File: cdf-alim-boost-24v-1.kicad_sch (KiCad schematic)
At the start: 89 parts, among them J1 Conn_01x02, J2 Conn_01x02, J3 Conn_01x02, Q1 BSC019N04LS, Q2 BSC019N04LS, Q3 BSC019N04LS, Q4 BSC019N04LS, Q5 BSC019N04LS, U1 HT753-1, U2 TPS25983, U4 LM5122

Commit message: schem: add boost shunt filter rc
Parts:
- added C34: 0n1, Capacitor_SMD:C_0402_1005Metric, symbol Device:C
- added R24, R25: 100, Resistor_SMD:R_0402_1005Metric, symbol Device:R
- C24: footprint Capacitor_SMD:C_0603_1608Metric_Pad1.08x0.95mm_HandSolder -> Resistor_SMD:R_0603_1608Metric
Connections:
- net +18V: now also R24.1; no longer U4.4 (CSP)
- net at L1.1, R16.2, TP12.1: now also R25.1; no longer U4.3 (CSN)
- new net: C34.2, R25.2, U4.3 (CSN)
- new net: C34.1, R24.2, U4.4 (CSP)

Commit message: schem: remove ilim testpoint
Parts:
- removed TP8: TestPoint, TestPoint:TestPoint_Pad_D2.0mm, symbol Connector:TestPoint_Small
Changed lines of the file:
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@@
 	)
 	(junction
-		(at 78.74 104.14)
-		(diameter 0)
-		(color 0 0 0 0)
-	)
-	(junction
 		(at 123.19 29.21)
 		(diameter 0)
@@
 					(unit 1)
 				)
-			)
-		)
-	)
-	(symbol
-		(lib_id "Connector:TestPoint_Small")
-		(at 78.74 104.14 270)
-		(unit 1)
-		(body_style 1)
-		(exclude_from_sim no)
-		(in_bom no)
-		(on_board yes)
-		(in_pos_files yes)
-		(dnp no)
-		(property "Reference" "TP8"
-			(at 73.66 102.87 90)
-			(show_name no)
-			(do_not_autoplace no)
-			(effects
-				(font
-					(size 1.27 1.27)
-				)
-				(justify left)
-			)
-		)
-		(property "Value" "TestPoint"
-			(at 80.7721 106.68 0)
-			(hide yes)
-			(show_name no)
-			(do_not_autoplace no)
-			(effects
-				(font
-					(size 1.27 1.27)
-				)
-				(justify left)
-			)
-		)
-		(property "Footprint" "TestPoint:TestPoint_Pad_D2.0mm"
-			(at 78.74 109.22 0)
-			(hide yes)
-			(show_name no)
-			(do_not_autoplace no)
-			(effects
-				(font
-					(size 1.27 1.27)
-				)
-			)
-		)
-		(property "Datasheet" ""
-			(at 78.74 109.22 0)
-			(hide yes)
-			(show_name no)
-			(do_not_autoplace no)
-			(effects
-				(font
-					(size 1.27 1.27)
-				)
-			)
-		)
-		(property "Description" "test point"
-			(at 78.74 104.14 0)
-			(hide yes)
-			(show_name no)
-			(do_not_autoplace no)
-			(effects
-				(font
-					(size 1.27 1.27)
-				)
-			)
-		)
-		(pin "1"
-		)
-		(instances
-			(project "cdf-alim-boost-24v-1"
-				(path "/c1d68e1e-31aa-4338-bfd5-3714fe43b2c6"
-					(reference "TP8")
-					(unit 1)
-				)

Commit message: schem: add assembly and mounting holes
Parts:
- added FID1, FID2, FID3: Fiducial, Fiducial:Fiducial_1mm_Mask2mm, symbol Mechanical:Fiducial
- added H1, H2, H3: MountingHole, MountingHole:ToolingHole_1.152mm, symbol Mechanical:MountingHole
- added H4, H5, H6, H7: MountingHole_Pad, MountingHole:MountingHole_3.2mm_M3_Pad_Via, symbol Mechanical:MountingHole_Pad
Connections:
- net AGND: now also H4.1, H5.1, H6.1, H7.1
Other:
- note added: "Mounting"
- note added: "SMT assembly"

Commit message: schem: remove extra +18v testpoint
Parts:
- removed TP11: TestPoint, TestPoint:TestPoint_Pad_D2.0mm, symbol Connector:TestPoint
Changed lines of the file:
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@@
 	)
 	(junction
-		(at 143.51 29.21)
-		(diameter 0)
-		(color 0 0 0 0)
-	)
-	(junction
 		(at 95.25 29.21)
 		(diameter 0)
@@
 	(wire
 		(pts
-			(xy 123.19 29.21) (xy 143.51 29.21)
-		)
-		(stroke
-			(width 0)
-			(type default)
-		)
-	)
-	(wire
-		(pts
 			(xy 31.75 38.1) (xy 31.75 39.37)
 		)
@@
 	(wire
 		(pts
-			(xy 143.51 29.21) (xy 156.21 29.21)
+			(xy 123.19 29.21) (xy 156.21 29.21)
 		)
 		(stroke
@@
 					(unit 1)
 				)
-			)
-		)
-	)
-	(symbol
-		(lib_id "Connector:TestPoint")
-		(at 143.51 29.21 0)
-		(unit 1)
-		(body_style 1)
-		(exclude_from_sim no)
-		(in_bom no)
-		(on_board yes)
-		(in_pos_files yes)
-		(dnp no)
-		(property "Reference" "TP11"
-			(at 141.986 23.876 0)
-			(show_name no)
-			(do_not_autoplace no)
-			(effects
-				(font
-					(size 1.27 1.27)
-				)
-				(justify left)
-			)
-		)
-		(property "Value" "TestPoint"
-			(at 146.05 27.1779 0)
-			(hide yes)
-			(show_name no)
-			(do_not_autoplace no)
-			(effects
-				(font
-					(size 1.27 1.27)
-				)
-				(justify left)
-			)
-		)
-		(property "Footprint" "TestPoint:TestPoint_Pad_D2.0mm"
-			(at 148.59 29.21 0)
-			(hide yes)
-			(show_name no)
-			(do_not_autoplace no)
-			(effects
-				(font
-					(size 1.27 1.27)
-				)
-			)
-		)
-		(property "Datasheet" ""
-			(at 148.59 29.21 0)
-			(hide yes)
-			(show_name no)
-			(do_not_autoplace no)
-			(effects
-				(font
-					(size 1.27 1.27)
-				)
-			)
-		)
-		(property "Description" "test point"
-			(at 143.51 29.21 0)
-			(hide yes)
-			(show_name no)
-			(do_not_autoplace no)
-			(effects
-				(font
-					(size 1.27 1.27)
-				)
-			)
-		)
-		(pin "1"
-		)
-		(instances
-			(project "cdf-alim-boost-24v-1"
-				(path "/c1d68e1e-31aa-4338-bfd5-3714fe43b2c6"
-					(reference "TP11")
-					(unit 1)
-				)

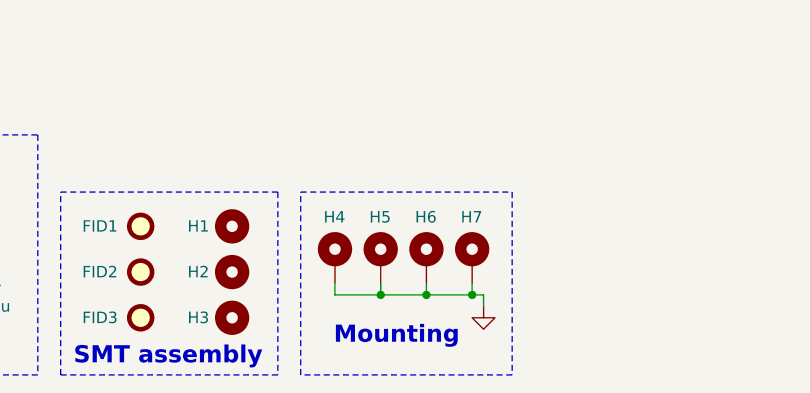
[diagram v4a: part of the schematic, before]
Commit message: schem: remove 1 mouting hole
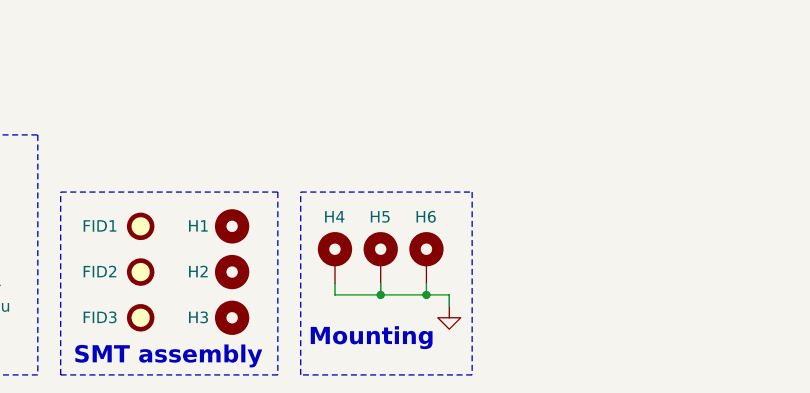
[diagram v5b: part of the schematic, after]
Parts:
- removed H7: MountingHole_Pad, MountingHole:MountingHole_3.2mm_M3_Pad_Via, symbol Mechanical:MountingHole_Pad
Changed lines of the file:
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@@
 	(rectangle
 		(start 87.63 175.26)
-		(end 111.125 195.58)
+		(end 106.68 195.58)
 		(stroke
 			(width 0)
@@
 	(text "Mounting"
 		(exclude_from_sim no)
-		(at 98.298 191.262 0)
+		(at 95.504 191.516 0)
 		(effects
 			(font
@@
 	)
 	(junction
-		(at 106.68 186.69)
-		(diameter 0)
-		(color 0 0 0 0)
-	)
-	(junction
 		(at 48.26 104.14)
 		(diameter 0)
@@
 	(wire
 		(pts
-			(xy 106.68 185.42) (xy 106.68 186.69)
-		)
-		(stroke
-			(width 0)
-			(type default)
-		)
-	)
-	(wire
-		(pts
 			(xy 213.36 29.21) (xy 218.44 29.21)
 		)
@@
 	(wire
 		(pts
-			(xy 106.68 186.69) (xy 107.95 186.69)
-		)
-		(stroke
-			(width 0)
-			(type default)
-		)
-	)
-	(wire
-		(pts
 			(xy 91.44 186.69) (xy 96.52 186.69)
 		)
@@
 	(wire
 		(pts
-			(xy 107.95 186.69) (xy 107.95 187.96)
+			(xy 104.14 186.69) (xy 104.14 187.96)
 		)
 		(stroke
@@
 	(wire
 		(pts
-			(xy 96.52 186.69) (xy 106.68 186.69)
+			(xy 96.52 186.69) (xy 104.14 186.69)
 		)
 		(stroke
@@
 	(symbol
 		(lib_id "power:GND")
-		(at 107.95 187.96 0)
+		(at 104.14 187.96 0)
 		(unit 1)
 		(body_style 1)
@@
 		(dnp no)
 		(property "Reference" "#PWR051"
-			(at 107.95 194.31 0)
+			(at 104.14 194.31 0)
 			(hide yes)
 			(show_name no)
@@
 		)
 		(property "Value" "GND"
-			(at 107.696 192.532 0)
+			(at 103.886 192.532 0)
 			(hide yes)
 			(show_name no)
@@
 		)
 		(property "Footprint" ""
-			(at 107.95 187.96 0)
+			(at 104.14 187.96 0)
 			(hide yes)
 			(show_name no)
@@
 		)
 		(property "Datasheet" ""
-			(at 107.95 187.96 0)
+			(at 104.14 187.96 0)
 			(hide yes)
 			(show_name no)
@@
 		)
 		(property "Description" "Power symbol creates a global label with name \"GND\" , ground"
-			(at 107.95 187.96 0)
+			(at 104.14 187.96 0)
 			(hide yes)
 			(show_name no)
@@
 					(unit 1)
 				)
-			)
-		)
-	)
-	(symbol
-		(lib_id "Mechanical:MountingHole_Pad")
-		(at 106.68 182.88 0)
-		(unit 1)
-		(body_style 1)
-		(exclude_from_sim no)
-		(in_bom no)
-		(on_board yes)
-		(in_pos_files yes)
-		(dnp no)
-		(property "Reference" "H7"
-			(at 105.41 178.054 0)
-			(show_name no)
-			(do_not_autoplace no)
-			(effects
-				(font
-					(size 1.27 1.27)
-				)
-				(justify left)
-			)
-		)
-		(property "Value" "MountingHole_Pad"
-			(at 110.49 181.61 90)
-			(hide yes)
-			(show_name no)
-			(do_not_autoplace no)
-			(effects
-				(font
-					(size 1.27 1.27)
-				)
-			)
-		)
-		(property "Footprint" "MountingHole:MountingHole_3.2mm_M3_Pad_Via"
-			(at 106.68 182.88 0)
-			(hide yes)
-			(show_name no)
-			(do_not_autoplace no)
-			(effects
-				(font
-					(size 1.27 1.27)
-				)
-			)
-		)
-		(property "Datasheet" ""
-			(at 106.68 182.88 0)
-			(hide yes)
-			(show_name no)
-			(do_not_autoplace no)
-			(effects
-				(font
-					(size 1.27 1.27)
-				)
-			)
-		)
-		(property "Description" "Mounting Hole with connection"
-			(at 106.68 182.88 0)
-			(hide yes)
-			(show_name no)
-			(do_not_autoplace no)
-			(effects
-				(font
-					(size 1.27 1.27)
-				)
-			)
-		)
-		(property "KLC_S3.3" ""
-			(at 106.68 182.88 0)
-			(hide yes)
-			(show_name no)
-			(do_not_autoplace no)
-			(effects
-				(font
-					(size 1.27 1.27)
-				)
-			)
-		)
-		(property "KLC_S4.1" ""
-			(at 106.68 182.88 0)
-			(hide yes)
-			(show_name no)
-			(do_not_autoplace no)
-			(effects
-				(font
-					(size 1.27 1.27)
-				)
-			)
-		)
-		(pin "1"
-		)
-		(instances
-			(project "cdf-alim-boost-24v-1"
-				(path "/c1d68e1e-31aa-4338-bfd5-3714fe43b2c6"
-					(reference "H7")
-					(unit 1)
-				)

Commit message: schem: fix 22n cap BOM
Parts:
- C8: JLCPCB Part # C1538 -> C1532; Manufacturer Part Number 0402B472K500NT -> 0402B223K500NT
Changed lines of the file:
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@@
 			)
 		)
-		(property "JLCPCB Part #" "C1538"
+		(property "JLCPCB Part #" "C1532"
 			(at 87.63 104.14 0)
 			(hide yes)
@@
 			)
 		)
-		(property "Manufacturer Part Number" "0402B472K500NT"
+		(property "Manufacturer Part Number" "0402B223K500NT"
 			(at 87.63 104.14 0)
 			(hide yes)
